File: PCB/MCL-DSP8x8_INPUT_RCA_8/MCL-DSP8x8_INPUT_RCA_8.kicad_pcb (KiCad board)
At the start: 2 copper layers, 80 x 40 mm, 16 parts, among them J1 Conn_01x05, J2 Conn_01x05, J3 Conn_01x05, J4 Conn_01x05

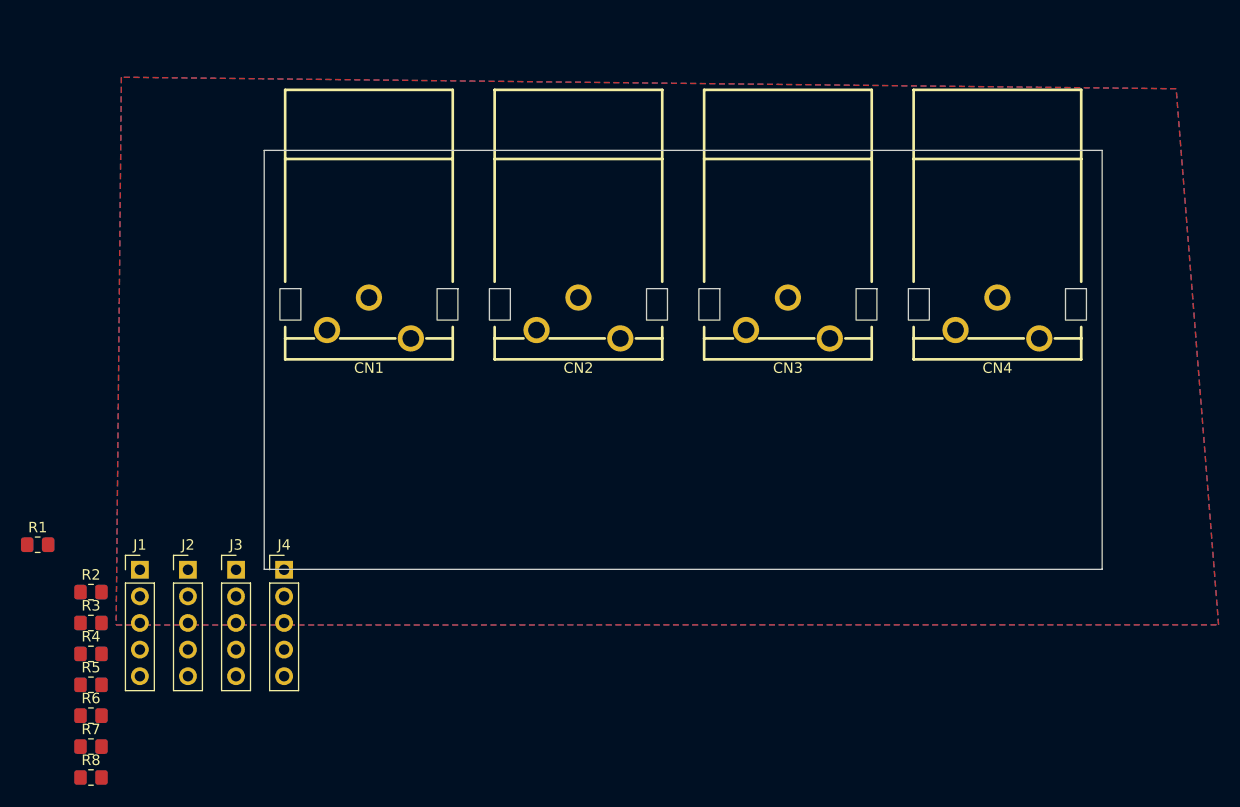
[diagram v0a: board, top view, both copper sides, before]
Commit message: Finished design of v1 connector boards.
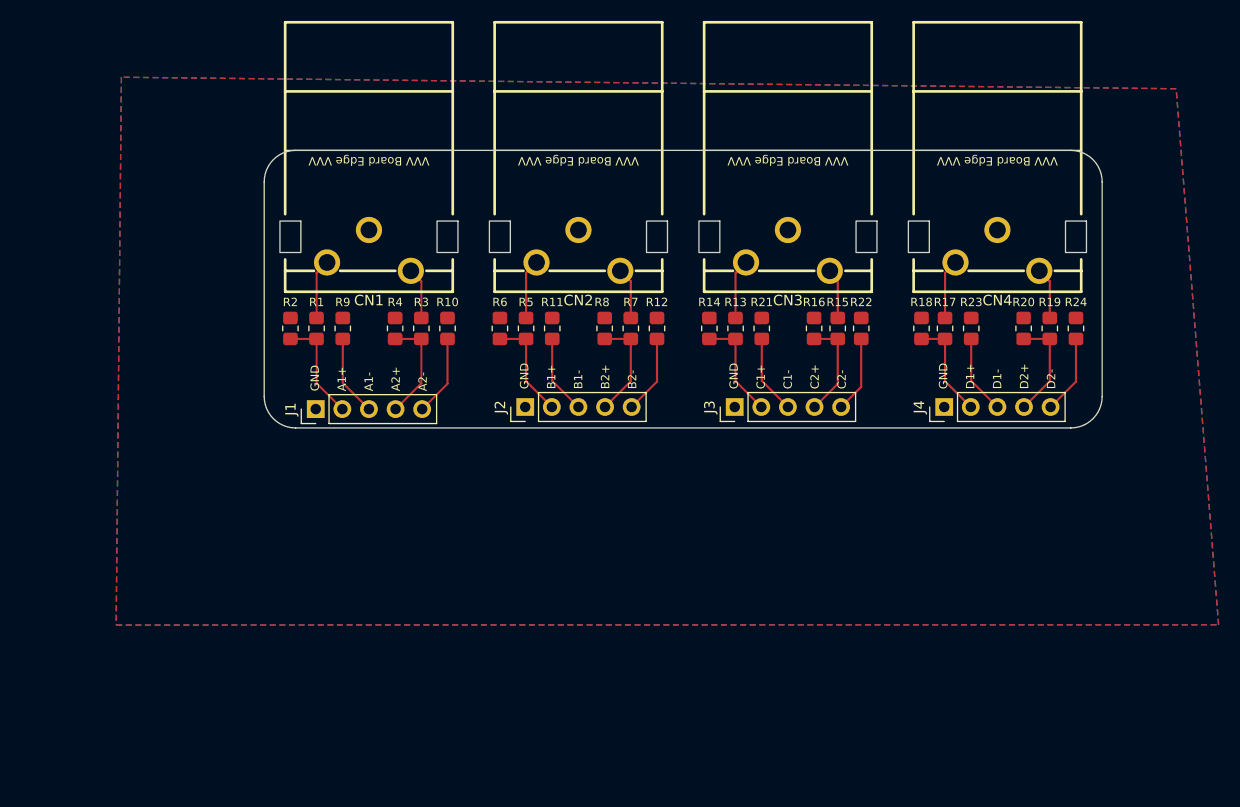
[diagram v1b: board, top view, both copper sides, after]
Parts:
- added R1: 82k, Resistor_SMD:R_0805_2012Metric_Pad1.20x1.40mm_HandSolder, F.Cu at (55.0, 67.0)
- added R13: 82k, Resistor_SMD:R_0805_2012Metric_Pad1.20x1.40mm_HandSolder, F.Cu at (95.0, 67.0)
- added R14: 10k, Resistor_SMD:R_0805_2012Metric_Pad1.20x1.40mm_HandSolder, F.Cu at (92.5, 67.0)
- added R15: 82k, Resistor_SMD:R_0805_2012Metric_Pad1.20x1.40mm_HandSolder, F.Cu at (104.8, 67.0)
- added R16: 10k, Resistor_SMD:R_0805_2012Metric_Pad1.20x1.40mm_HandSolder, F.Cu at (102.5, 67.0)
- added R17: 82k, Resistor_SMD:R_0805_2012Metric_Pad1.20x1.40mm_HandSolder, F.Cu at (115.0, 67.0)
- added R18: 10k, Resistor_SMD:R_0805_2012Metric_Pad1.20x1.40mm_HandSolder, F.Cu at (112.8, 67.0)
- added R19: 82k, Resistor_SMD:R_0805_2012Metric_Pad1.20x1.40mm_HandSolder, F.Cu at (125.0, 67.0)
- added R2: 10k, Resistor_SMD:R_0805_2012Metric_Pad1.20x1.40mm_HandSolder, F.Cu at (52.5, 67.0)
- added R20: 10k, Resistor_SMD:R_0805_2012Metric_Pad1.20x1.40mm_HandSolder, F.Cu at (122.5, 67.0)
- added R3: 82k, Resistor_SMD:R_0805_2012Metric_Pad1.20x1.40mm_HandSolder, F.Cu at (65.0, 67.0)
- added R4: 10k, Resistor_SMD:R_0805_2012Metric_Pad1.20x1.40mm_HandSolder, F.Cu at (62.5, 67.0)
- added R5: 82k, Resistor_SMD:R_0805_2012Metric_Pad1.20x1.40mm_HandSolder, F.Cu at (75.0, 67.0)
- added R6: 10k, Resistor_SMD:R_0805_2012Metric_Pad1.20x1.40mm_HandSolder, F.Cu at (72.5, 67.0)
- added R7: 82k, Resistor_SMD:R_0805_2012Metric_Pad1.20x1.40mm_HandSolder, F.Cu at (85.0, 67.0)
- added R8: 10k, Resistor_SMD:R_0805_2012Metric_Pad1.20x1.40mm_HandSolder, F.Cu at (82.5, 67.0)
- moved R24 102.2 mm to (127.5, 67.0), turned to 90 degrees
- moved R23 90.7 mm to (117.5, 67.0), turned to 90 degrees
- moved R22 79.8 mm to (107.0, 67.0), turned to 90 degrees
- moved R21 69.9 mm to (97.5, 67.0), turned to 90 degrees
- moved J4 64.9 mm to (114.9, 74.5), turned to 90 degrees
- moved R12 59.6 mm to (87.5, 67.0), turned to 90 degrees
- moved R10 54.7 mm to (67.5, 67.0), turned to 90 degrees
- moved R11 53.3 mm to (77.5, 67.0), turned to 90 degrees
- moved J3 50.1 mm to (94.9, 74.5), turned to 90 degrees
- moved R9 44.1 mm to (57.5, 67.0), turned to 90 degrees
- moved J2 35.8 mm to (74.9, 74.5), turned to 90 degrees
- moved J1 22.7 mm to (54.9, 74.7), turned to 90 degrees
- moved CN1 6.45 mm to (60.0, 59.5)
- moved CN2 6.45 mm to (80.0, 59.5)
- moved CN3 6.45 mm to (100.0, 59.5)
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- renumbered R8 to R10, R1 to R11, R2 to R12, R3 to R21, R4 to R22, R5 to R23, R7 to R24, R6 to R9
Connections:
- CN1 pad 1: /A2+ -> /RCA_A2+
- CN1 pad 3: /A1+ -> /RCA_A1+
- CN2 pad 1: /B2+ -> /RCA_B2+
- CN2 pad 3: /B1+ -> /RCA_B1+
- CN3 pad 1: /C2+ -> /RCA_C2+
- CN3 pad 3: /C1+ -> /RCA_C1+
- CN4 pad 1: /D2+ -> /RCA_D2+
- CN4 pad 3: /D1+ -> /RCA_D1+
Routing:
- net /A1+: track 0.00 -> 10.5 mm
- net /A2+: track 0.00 -> 10.2 mm
- net /D2+: track 0.00 -> 10.0 mm
- net /C1+: track 0.00 -> 10.0 mm
- net /B2+: track 0.00 -> 10.0 mm
- net /B1+: track 0.00 -> 10.0 mm
- net /D1+: track 0.00 -> 9.77 mm
- net /C2+: track 0.00 -> 9.67 mm
- net /A1-: track 0.00 -> 7.74 mm
- net /A2-: track 0.00 -> 7.70 mm
- net /D1-: track 0.00 -> 7.54 mm
- net /C1-: track 0.00 -> 7.54 mm
- net /B1-: track 0.00 -> 7.54 mm
- net /D2-: track 0.00 -> 7.50 mm
- net /B2-: track 0.00 -> 7.50 mm
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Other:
- board size 80 x 40 mm -> 80 x 26.5 mm
- board text added: "Eight-Channel RCA Input V1 Designed for MCL-DSP8x8"
- board text added: "GND A1+ A1- A2+ A2-"
- board text added: "GND B1+ B1- B2+ B2-"
- board text added: "GND C1+ C1- C2+ C2-"
- board text added: "GND D1+ D1- D2+ D2-"
